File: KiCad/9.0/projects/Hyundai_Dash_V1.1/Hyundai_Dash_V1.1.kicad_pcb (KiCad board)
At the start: 2 copper layers, 109 x 64 mm, 30 parts, among them J1 +12V-GND, J10 GND-Fuel, J2 IGN-LSG-RSG-LS1-LS2, J3 C-CAN, J4 C-CAN, J5 C-CAN SPI, J6 B-CAN, J7 B-CAN, J8 B-CAN SPI, J9 Jumper Holder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

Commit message: KiCad: Hyundai_Dash_V1.1: remove jumper holder
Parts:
- removed J9: Jumper Holder, Connector_PinHeader_2.54mm:PinHeader_1x02_P2.54mm_Vertical

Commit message: KiCad: Hyundai_Dash_V1.1: reassign annotations
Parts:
- J2: value IGN-LSG-RSG-LS1-LS2 -> IGN-HS1-HS2-LS1-LS2
- renumbered J10 to J9
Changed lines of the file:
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@@
 	(net 55 "Net-(U2-I4)")
 	(net 56 "Net-(U2-I1)")
-	(net 57 "unconnected-(U3-QH&apos;-Pad9)")
-	(net 58 "Net-(J10-Pin_2)")
+	(net 57 "Net-(J9-Pin_2)")
+	(net 58 "unconnected-(U3-QH'-Pad9)")
 	(net 59 "unconnected-(U1-O6-Pad13)")
 	(net 60 "unconnected-(U1-I6-Pad6)")
@@
 		(property ki_fp_filters "Connector*:*_1x??_*")
 		(sheetname "/")
-		(sheetfile "Hyundai_Dash_V1.kicad_sch")
+		(sheetfile "Hyundai_Dash_V1.1.kicad_sch")
 		(attr through_hole exclude_from_bom)
 		(fp_line
@@
 		(property ki_fp_filters "R_*")
 		(sheetname "/")
-		(sheetfile "Hyundai_Dash_V1.kicad_sch")
+		(sheetfile "Hyundai_Dash_V1.1.kicad_sch")
 		(attr smd)
 		(fp_line
@@
 		(property ki_fp_filters "Connector*:*_1x??_*")
 		(sheetname "/")
-		(sheetfile "Hyundai_Dash_V1.kicad_sch")
+		(sheetfile "Hyundai_Dash_V1.1.kicad_sch")
 		(attr through_hole exclude_from_bom)
 		(fp_line
@@
 		(property ki_fp_filters "R_*")
 		(sheetname "/")
-		(sheetfile "Hyundai_Dash_V1.kicad_sch")
+		(sheetfile "Hyundai_Dash_V1.1.kicad_sch")
 		(attr smd)
 		(fp_line
@@
 			(layers "F.Cu" "F.Mask" "F.Paste")
 			(roundrect_rratio 0.204082)
-			(net 58 "Net-(J10-Pin_2)")
+			(net 57 "Net-(J9-Pin_2)")
 			(pintype "passive")
 		)
@@
 		(property ki_fp_filters "C_*")
 		(sheetname "/")
-		(sheetfile "Hyundai_Dash_V1.kicad_sch")
+		(sheetfile "Hyundai_Dash_V1.1.kicad_sch")
 		(attr smd)
 		(fp_line
@@
 		(property ki_fp_filters "TO?220*")
 		(sheetname "/")
-		(sheetfile "Hyundai_Dash_V1.kicad_sch")
+		(sheetfile "Hyundai_Dash_V1.1.kicad_sch")
 		(attr through_hole exclude_from_bom)
 		(fp_line
@@
 		(property ki_fp_filters "R_*")
 		(sheetname "/")
-		(sheetfile "Hyundai_Dash_V1.kicad_sch")
+		(sheetfile "Hyundai_Dash_V1.1.kicad_sch")
 		(attr smd)
 		(fp_line
@@
 			(layers "F.Cu" "F.Mask" "F.Paste")
 			(roundrect_rratio 0.204082)
-			(net 58 "Net-(J10-Pin_2)")
+			(net 57 "Net-(J9-Pin_2)")
 			(pintype "passive")
 		)
@@
 		(property ki_fp_filters "Connector*:*_1x??_*")
 		(sheetname "/")
-		(sheetfile "Hyundai_Dash_V1.kicad_sch")
+		(sheetfile "Hyundai_Dash_V1.1.kicad_sch")
 		(attr through_hole exclude_from_bom)
 		(fp_line
@@
 		(property ki_fp_filters "R_*")
 		(sheetname "/")
-		(sheetfile "Hyundai_Dash_V1.kicad_sch")
+		(sheetfile "Hyundai_Dash_V1.1.kicad_sch")
 		(attr smd)
 		(fp_line
@@
 			(layers "F.Cu" "F.Mask" "F.Paste")
 			(roundrect_rratio 0.204082)
-			(net 58 "Net-(J10-Pin_2)")
+			(net 57 "Net-(J9-Pin_2)")
 			(pintype "passive")
 		)
@@
 		(property ki_fp_filters "DIP*W7.62mm* SOIC*7.5x11.6mm*P1.27mm*")
 		(sheetname "/")
-		(sheetfile "Hyundai_Dash_V1.kicad_sch")
+		(sheetfile "Hyundai_Dash_V1.1.kicad_sch")
 		(attr through_hole exclude_from_bom)
 		(fp_line
@@
 		(property ki_fp_filters "R_*")
 		(sheetname "/")
-		(sheetfile "Hyundai_Dash_V1.kicad_sch")
+		(sheetfile "Hyundai_Dash_V1.1.kicad_sch")
 		(attr smd)
 		(fp_line
@@
 			(layers "F.Cu" "F.Mask" "F.Paste")
 			(roundrect_rratio 0.204082)
-			(net 58 "Net-(J10-Pin_2)")
+			(net 57 "Net-(J9-Pin_2)")
 			(pintype "passive")
 		)
@@
 		(descr "JST XH series connector, B2B-XH-A (http://www.jst-mfg.com/product/pdf/eng/eXH.pdf), generated with kicad-footprint-generator")
 		(tags "connector JST XH vertical")
-		(property "Reference" "J10"
+		(property "Reference" "J9"
 			(at 1.25 -3.55 0)
 			(layer "F.SilkS")
@@
 		(property ki_fp_filters "Connector*:*_1x??_*")
 		(sheetname "/")
-		(sheetfile "Hyundai_Dash_V1.kicad_sch")
+		(sheetfile "Hyundai_Dash_V1.1.kicad_sch")
 		(attr through_hole exclude_from_bom)
 		(fp_line
@@
 			(layers "*.Cu" "*.Mask")
 			(remove_unused_layers no)
-			(net 58 "Net-(J10-Pin_2)")
+			(net 57 "Net-(J9-Pin_2)")
 			(pinfunction "Pin_2")
 			(pintype "passive")
@@
 		(property ki_fp_filters "Connector*:*_1x??_*")
 		(sheetname "/")
-		(sheetfile "Hyundai_Dash_V1.kicad_sch")
+		(sheetfile "Hyundai_Dash_V1.1.kicad_sch")
 		(attr through_hole exclude_from_bom)
 		(fp_line
@@
 		(property ki_fp_filters "DIP*W7.62mm* SOIC*7.5x11.6mm*P1.27mm*")
 		(sheetname "/")
-		(sheetfile "Hyundai_Dash_V1.kicad_sch")
+		(sheetfile "Hyundai_Dash_V1.1.kicad_sch")
 		(attr through_hole exclude_from_bom)
 		(fp_line
@@
 		(property ki_fp_filters "R_*")
 		(sheetname "/")
-		(sheetfile "Hyundai_Dash_V1.kicad_sch")
+		(sheetfile "Hyundai_Dash_V1.1.kicad_sch")
 		(attr smd)
 		(fp_line
@@
 			(layers "F.Cu" "F.Mask" "F.Paste")
 			(roundrect_rratio 0.204082)
-			(net 58 "Net-(J10-Pin_2)")
+			(net 57 "Net-(J9-Pin_2)")
 			(pintype "passive")
 		)
@@
 		(property ki_fp_filters "Arduino*Nano*")
 		(sheetname "/")
-		(sheetfile "Hyundai_Dash_V1.kicad_sch")
+		(sheetfile "Hyundai_Dash_V1.1.kicad_sch")
 		(attr through_hole exclude_from_bom)
 		(fp_line
@@
 		(property ki_fp_filters "Connector*:*_1x??_*")
 		(sheetname "/")
-		(sheetfile "Hyundai_Dash_V1.kicad_sch")
+		(sheetfile "Hyundai_Dash_V1.1.kicad_sch")
 		(attr through_hole exclude_from_bom)
 		(fp_line
@@
 		(property ki_fp_filters "R_*")
 		(sheetname "/")
-		(sheetfile "Hyundai_Dash_V1.kicad_sch")
+		(sheetfile "Hyundai_Dash_V1.1.kicad_sch")
 		(attr smd)
 		(fp_line
@@
 			(layers "F.Cu" "F.Mask" "F.Paste")
 			(roundrect_rratio 0.204082)
-			(net 58 "Net-(J10-Pin_2)")
+			(net 57 "Net-(J9-Pin_2)")
 			(pintype "passive")
 		)
@@
 		(property ki_fp_filters "Connector*:*_1x??_*")
 		(sheetname "/")
-		(sheetfile "Hyundai_Dash_V1.kicad_sch")
+		(sheetfile "Hyundai_Dash_V1.1.kicad_sch")
 		(attr through_hole exclude_from_bom)
 		(fp_line
@@
 		(property ki_fp_filters "TO?92*")
 		(sheetname "/")
-		(sheetfile "Hyundai_Dash_V1.kicad_sch")
+		(sheetfile "Hyundai_Dash_V1.1.kicad_sch")
 		(attr through_hole)
 		(fp_line
@@
 		(property ki_fp_filters "Connector*:*_1x??_*")
 		(sheetname "/")
-		(sheetfile "Hyundai_Dash_V1.kicad_sch")
+		(sheetfile "Hyundai_Dash_V1.1.kicad_sch")
 		(attr through_hole exclude_from_bom)
 		(fp_line
@@
 			)
 		)
-		(property "Value" "IGN-LSG-RSG-LS1-LS2"
+		(property "Value" "IGN-HS1-HS2-LS1-LS2"
 			(at 5 4.6 0)
 			(layer "F.SilkS")
@@
 		(property ki_fp_filters "Connector*:*_1x??_*")
 		(sheetname "/")
-		(sheetfile "Hyundai_Dash_V1.kicad_sch")
+		(sheetfile "Hyundai_Dash_V1.1.kicad_sch")
 		(attr through_hole)
 		(fp_line
@@
 		(property ki_fp_filters "R_*")
 		(sheetname "/")
-		(sheetfile "Hyundai_Dash_V1.kicad_sch")
+		(sheetfile "Hyundai_Dash_V1.1.kicad_sch")
 		(attr smd)
 		(fp_line
@@
 			(layers "F.Cu" "F.Mask" "F.Paste")
 			(roundrect_rratio 0.204082)
-			(net 58 "Net-(J10-Pin_2)")
+			(net 57 "Net-(J9-Pin_2)")
 			(pintype "passive")
 		)
@@
 		(property ki_fp_filters "TO?92*")
 		(sheetname "/")
-		(sheetfile "Hyundai_Dash_V1.kicad_sch")
+		(sheetfile "Hyundai_Dash_V1.1.kicad_sch")
 		(attr through_hole)
 		(fp_line
@@
 		(property ki_fp_filters "*Buzzer*")
 		(sheetname "/")
-		(sheetfile "Hyundai_Dash_V1.kicad_sch")
+		(sheetfile "Hyundai_Dash_V1.1.kicad_sch")
 		(attr through_hole exclude_from_bom)
 		(fp_circle
@@
 		(property ki_fp_filters "R_*")
 		(sheetname "/")
-		(sheetfile "Hyundai_Dash_V1.kicad_sch")
+		(sheetfile "Hyundai_Dash_V1.1.kicad_sch")
 		(attr smd)
 		(fp_line
@@
 			(layers "F.Cu" "F.Mask" "F.Paste")
 			(roundrect_rratio 0.204082)
-			(net 58 "Net-(J10-Pin_2)")
+			(net 57 "Net-(J9-Pin_2)")
 			(pintype "passive")
 		)
@@
 		(property ki_fp_filters "R_*")
 		(sheetname "/")
-		(sheetfile "Hyundai_Dash_V1.kicad_sch")
+		(sheetfile "Hyundai_Dash_V1.1.kicad_sch")
 		(attr smd)
 		(fp_line
@@
 		(property ki_fp_filters "DIP*W7.62mm* SOIC*3.9x9.9mm*P1.27mm* TSSOP*4.4x5mm*P0.65mm* SOIC*5.3x10.2mm*P1.27mm* SOIC*7.5x10.3mm*P1.27mm*")
 		(sheetname "/")
-		(sheetfile "Hyundai_Dash_V1.kicad_sch")
+		(sheetfile "Hyundai_Dash_V1.1.kicad_sch")
 		(attr through_hole exclude_from_bom)
 		(fp_line
@@
 			(layers "*.Cu" "*.Mask")
 			(remove_unused_layers no)
-			(net 57 "unconnected-(U3-QH&apos;-Pad9)")
+			(net 58 "unconnected-(U3-QH'-Pad9)")
 			(pinfunction "QH'")
 			(pintype "output+no_connect")
@@
 		(property ki_fp_filters "R_*")
 		(sheetname "/")
-		(sheetfile "Hyundai_Dash_V1.kicad_sch")
+		(sheetfile "Hyundai_Dash_V1.1.kicad_sch")
 		(attr smd)
 		(fp_line
@@
 		(locked yes)
 		(layer "F.Cu")
-		(net 58)
+		(net 57)
 	)
 	(segment
@@
 		(locked yes)
 		(layer "F.Cu")
-		(net 58)
+		(net 57)
 	)
 	(segment
@@
 		(locked yes)
 		(layer "F.Cu")
-		(net 58)
+		(net 57)
 	)
 	(segment
@@
 		(locked yes)
 		(layer "F.Cu")
-		(net 58)
+		(net 57)
 	)
 	(segment
@@
 		(locked yes)
 		(layer "F.Cu")
-		(net 58)
+		(net 57)
 	)
 	(segment
@@
 		(locked yes)
 		(layer "F.Cu")
-		(net 58)
+		(net 57)
 	)
 	(segment
@@
 		(locked yes)
 		(layer "F.Cu")
-		(net 58)
+		(net 57)
 	)
 	(segment
@@
 		(locked yes)
 		(layer "F.Cu")
-		(net 58)
+		(net 57)
 	)
 	(segment
@@
 		(locked yes)
 		(layer "F.Cu")
-		(net 58)
+		(net 57)
 	)
 	(segment
@@
 		(locked yes)
 		(layer "F.Cu")
-		(net 58)
+		(net 57)
 	)
 	(segment
@@
 		(locked yes)
 		(layer "F.Cu")
-		(net 58)
+		(net 57)
 	)
 	(segment

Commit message: KiCad: Hyundai_Dash_V1.1: update U1-U3 footprints to non-socketed versions
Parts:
- U1, U2: footprint Package_DIP:DIP-18_W7.62mm_Socket -> Package_DIP:DIP-18_W7.62mm
- U3: footprint Package_DIP:DIP-16_W7.62mm_Socket -> Package_DIP:DIP-16_W7.62mm
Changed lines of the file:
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@@
 		)
 	)
-	(footprint "Package_DIP:DIP-18_W7.62mm_Socket"
+	(footprint "Package_DIP:DIP-18_W7.62mm"
 		(locked yes)
 		(layer "F.Cu")
 		(at 205.501824 61.419772)
-		(descr "18-lead though-hole mounted DIP package, row spacing 7.62mm (300 mils), Socket")
-		(tags "THT DIP DIL PDIP 2.54mm 7.62mm 300mil Socket")
+		(descr "18-lead though-hole mounted DIP package, row spacing 7.62mm (300 mils)")
+		(tags "THT DIP DIL PDIP 2.54mm 7.62mm 300mil")
 		(property "Reference" "U2"
 			(at 3.81 -2.33 0)
@@
 		)
 		(property "Value" "ULN2803A"
-			(at 3.81 -3.72 0)
+			(at 3.748176 -3.919772 0)
 			(layer "F.SilkS")
 			(effects
@@
 			)
 		)
-		(property "Datasheet" "http://www.ti.com/lit/ds/symlink/uln2803a.pdf"
+		(property "Datasheet" ""
 			(at 0 0 0)
 			(layer "F.Fab")
@@
 			)
 		)
-		(property "Description" "Darlington Transistor Arrays, SOIC18/DIP18"
+		(property "Description" ""
 			(at 0 0 0)
 			(layer "F.Fab")
@@
 		(sheetname "/")
 		(sheetfile "Hyundai_Dash_V1.1.kicad_sch")
-		(attr through_hole exclude_from_bom)
+		(attr through_hole)
 		(fp_line
 			(start 1.16 -1.33)
@@
 			(layer "F.SilkS")
 		)
-		(fp_rect
-			(start -1.33 -1.39)
-			(end 8.95 21.71)
-			(stroke
-				(width 0.12)
-				(type solid)
-			)
-			(fill no)
-			(layer "F.SilkS")
-		)
 		(fp_arc
 			(start 4.81 -1.33)
@@
 		)
 		(fp_rect
-			(start -1.52 -1.58)
-			(end 9.14 21.9)
+			(start -1.06 -1.52)
+			(end 8.67 21.84)
 			(stroke
 				(width 0.05)
@@
 			(layer "F.Fab")
 		)
-		(fp_rect
-			(start -1.27 -1.33)
-			(end 8.89 21.65)
-			(stroke
-				(width 0.1)
-				(type solid)
-			)
-			(fill no)
-			(layer "F.Fab")
-		)
 		(fp_text user "${REFERENCE}"
 			(at 3.81 10.16 90)
@@
 		)
 		(embedded_fonts no)
-		(model "${KICAD9_3DMODEL_DIR}/Package_DIP.3dshapes/DIP-18_W7.62mm_Socket.step"
+		(model "${KICAD9_3DMODEL_DIR}/Package_DIP.3dshapes/DIP-18_W7.62mm.step"
 			(offset
 				(xyz 0 0 0)
@@
 		)
 	)
-	(footprint "Package_DIP:DIP-18_W7.62mm_Socket"
+	(footprint "Package_DIP:DIP-18_W7.62mm"
 		(locked yes)
 		(layer "F.Cu")
 		(at 169.26 81.62 90)
-		(descr "18-lead though-hole mounted DIP package, row spacing 7.62mm (300 mils), Socket")
-		(tags "THT DIP DIL PDIP 2.54mm 7.62mm 300mil Socket")
+		(descr "18-lead though-hole mounted DIP package, row spacing 7.62mm (300 mils)")
+		(tags "THT DIP DIL PDIP 2.54mm 7.62mm 300mil")
 		(property "Reference" "U1"
 			(at 3.81 -2.33 90)
@@
 		)
 		(property "Value" "ULN2803A"
-			(at 10.12 3.24 180)
+			(at 9.62 2.49 180)
 			(layer "F.SilkS")
 			(effects
@@
 			)
 		)
-		(property "Datasheet" "http://www.ti.com/lit/ds/symlink/uln2803a.pdf"
+		(property "Datasheet" ""
 			(at 0 0 90)
 			(layer "F.Fab")
@@
 			)
 		)
-		(property "Description" "Darlington Transistor Arrays, SOIC18/DIP18"
+		(property "Description" ""
 			(at 0 0 90)
 			(layer "F.Fab")
@@
 		(sheetname "/")
 		(sheetfile "Hyundai_Dash_V1.1.kicad_sch")
-		(attr through_hole exclude_from_bom)
+		(attr through_hole)
 		(fp_line
 			(start 6.46 -1.33)
@@
 			(layer "F.SilkS")
 		)
-		(fp_rect
-			(start -1.33 -1.39)
-			(end 8.95 21.71)
-			(stroke
-				(width 0.12)
-				(type solid)
-			)
-			(fill no)
-			(layer "F.SilkS")
-		)
 		(fp_arc
 			(start 4.81 -1.33)
@@
 		)
 		(fp_rect
-			(start -1.52 -1.58)
-			(end 9.14 21.9)
+			(start -1.06 -1.52)
+			(end 8.67 21.84)
 			(stroke
 				(width 0.05)
@@
 			(layer "F.Fab")
 		)
-		(fp_rect
-			(start -1.27 -1.33)
-			(end 8.89 21.65)
-			(stroke
-				(width 0.1)
-				(type solid)
-			)
-			(fill no)
-			(layer "F.Fab")
-		)
 		(fp_text user "${REFERENCE}"
-			(at 3.81 10.16 0)
+			(at 3.81 10.16 180)
 			(layer "F.Fab")
 			(effects
@@
 		)
 		(embedded_fonts no)
-		(model "${KICAD9_3DMODEL_DIR}/Package_DIP.3dshapes/DIP-18_W7.62mm_Socket.step"
+		(model "${KICAD9_3DMODEL_DIR}/Package_DIP.3dshapes/DIP-18_W7.62mm.step"
 			(offset
 				(xyz 0 0 0)
@@
 		)
 	)
-	(footprint "Package_DIP:DIP-16_W7.62mm_Socket"
+	(footprint "Package_DIP:DIP-16_W7.62mm"
 		(locked yes)
 		(layer "F.Cu")
 		(at 202 79.2 180)
-		(descr "16-lead though-hole mounted DIP package, row spacing 7.62mm (300 mils), Socket")
-		(tags "THT DIP DIL PDIP 2.54mm 7.62mm 300mil Socket")
+		(descr "16-lead though-hole mounted DIP package, row spacing 7.62mm (300 mils)")
+		(tags "THT DIP DIL PDIP 2.54mm 7.62mm 300mil")
 		(property "Reference" "U3"
-			(at 3.81 20.110228 0)
-			(unlocked yes)
+			(at 3.75 20.2 180)
 			(layer "F.SilkS")
 			(effects
@@
 		)
 		(property "Value" "74HC595"
-			(at 3.81 21.500228 180)
+			(at 3.75 21.7 180)
 			(layer "F.SilkS")
 			(effects
@@
 			)
 		)
-		(property "Datasheet" "http://www.ti.com/lit/ds/symlink/sn74hc595.pdf"
-			(at 0 0 0)
+		(property "Datasheet" ""
+			(at 0 0 180)
 			(layer "F.Fab")
 			(hide yes)
@@
 			)
 		)
-		(property "Description" "8-bit serial in/out Shift Register 3-State Outputs"
-			(at 0 0 0)
+		(property "Description" ""
+			(at 0 0 180)
 			(layer "F.Fab")
 			(hide yes)
@@
 		(sheetname "/")
 		(sheetfile "Hyundai_Dash_V1.1.kicad_sch")
-		(attr through_hole exclude_from_bom)
+		(attr through_hole)
 		(fp_line
 			(start 6.46 19.11)
@@
 			(layer "F.SilkS")
 		)
-		(fp_rect
-			(start -1.33 -1.39)
-			(end 8.95 19.17)
-			(stroke
-				(width 0.12)
-				(type solid)
-			)
-			(fill no)
-			(layer "F.SilkS")
-		)
 		(fp_arc
 			(start 4.81 -1.33)
@@
 		)
 		(fp_rect
-			(start -1.52 -1.58)
-			(end 9.14 19.36)
+			(start -1.06 -1.52)
+			(end 8.67 19.3)
 			(stroke
 				(width 0.05)
@@
 			(layer "F.Fab")
 		)
-		(fp_rect
-			(start -1.27 -1.33)
-			(end 8.89 19.11)
-			(stroke
-				(width 0.1)
-				(type solid)
-			)
-			(fill no)
-			(layer "F.Fab")
-		)
 		(fp_text user "${REFERENCE}"
-			(at 3.81 8.89 90)
+			(at 3.81 8.89 270)
 			(layer "F.Fab")
 			(effects
@@
 		)
 		(embedded_fonts no)
-		(model "${KICAD9_3DMODEL_DIR}/Package_DIP.3dshapes/DIP-16_W7.62mm_Socket.step"
+		(model "${KICAD9_3DMODEL_DIR}/Package_DIP.3dshapes/DIP-16_W7.62mm.step"
 			(offset
 				(xyz 0 0 0)

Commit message: KiCad: Hyundai_Dash_V1.1: update silkscreen markings
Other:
- board text added: "Hyundai Dash V1.1"
- board text added: "github.com/eymenyg/hyundai_dash_v1"
- board text removed: "Hyundai Dash V1"

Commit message: KiCad: Hyundai_Dash_V1.1: fix C1 positioning and R4 connection width
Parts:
- moved C1 2.97 mm to (195.2, 83.0)
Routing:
- net +5V: track 106.9 -> 102.3 mm
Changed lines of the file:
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@@
 	(footprint "Capacitor_SMD:C_0603_1608Metric"
 		(layer "F.Cu")
-		(at 198.19 83.199772)
+		(at 195.225 83)
 		(descr "Capacitor SMD 0603 (1608 Metric), square (rectangular) end terminal, IPC-7351 nominal, (Body size source: IPC-SM-782 page 76, https://www.pcb-3d.com/wordpress/wp-content/uploads/ipc-sm-782a_amendment_1_and_2.pdf), generated with kicad-footprint-generator")
 		(tags "capacitor")
@@
 	)
 	(segment
-		(start 197.415 83.199772)
-		(end 196.699772 83.199772)
+		(start 123.116614 92.306195)
+		(end 123.193805 92.306195)
 		(width 0.2)
 		(layer "F.Cu")
@@
 	)
 	(segment
-		(start 196.699772 83.199772)
-		(end 194.38 80.88)
+		(start 164.68 92.38)
+		(end 165 92.38)
 		(width 0.2)
 		(layer "F.Cu")
@@
 	)
 	(segment
-		(start 194.38 80.88)
-		(end 194.38 79.2)
+		(start 154.04 81.74)
+		(end 155.3 83)
 		(width 0.2)
 		(layer "F.Cu")
@@
 	)
 	(segment
-		(start 123.116614 92.306195)
-		(end 123.193805 92.306195)
+		(start 155.3 83)
+		(end 164.68 92.38)
 		(width 0.2)
 		(layer "F.Cu")
@@
 	)
 	(segment
-		(start 164.68 92.38)
-		(end 165 92.38)
+		(start 194.45 83)
+		(end 155.3 83)
 		(width 0.2)
 		(layer "F.Cu")
@@
 	)
 	(segment
-		(start 154.04 81.74)
-		(end 164.68 92.38)
+		(start 194.38 79.2)
+		(end 194.38 82.93)
 		(width 0.2)
 		(layer "F.Cu")
@@
 	)
 	(segment
-		(start 197.415 83.199772)
-		(end 155.499772 83.199772)
+		(start 194.38 82.93)
+		(end 194.45 83)
 		(width 0.2)
 		(layer "F.Cu")
@@
 		(start 223.9625 53.9625)
 		(end 223.9625 56.09)
-		(width 0.2)
+		(width 0.4)
 		(layer "F.Cu")
 		(net 57)

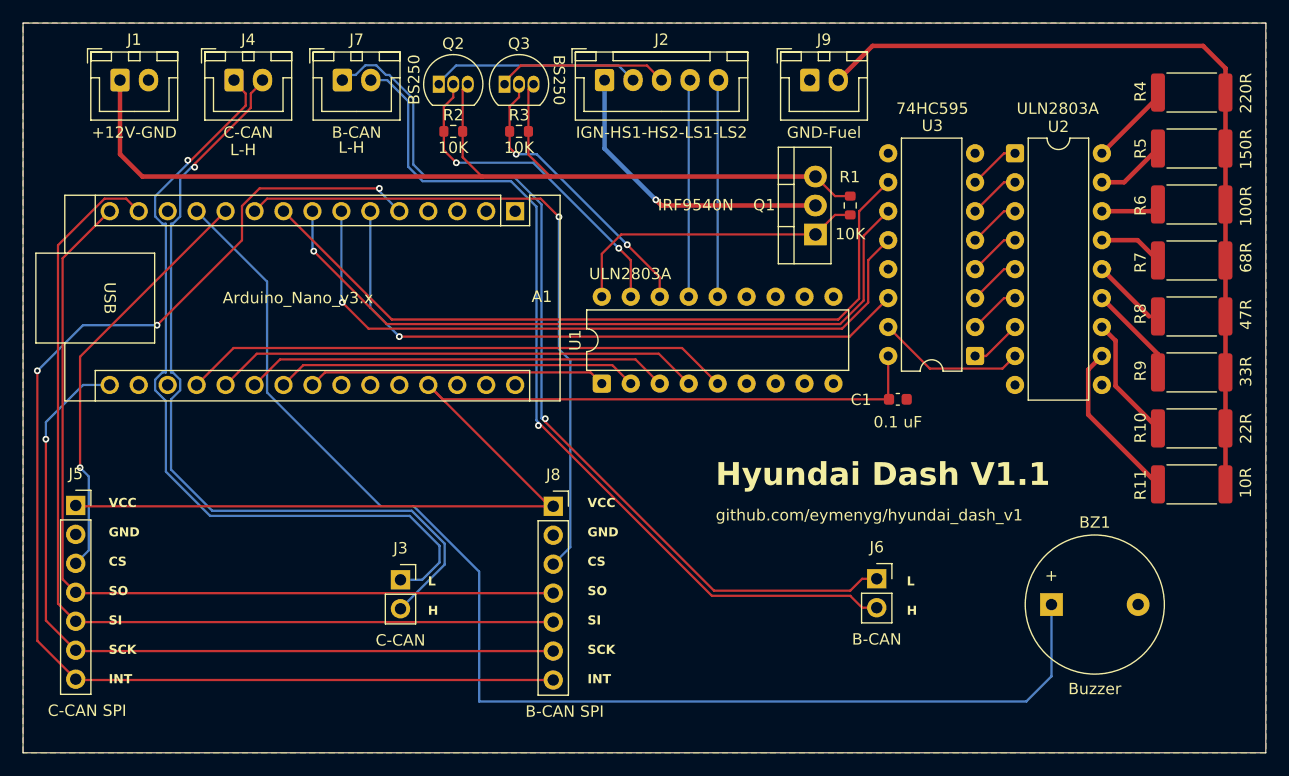
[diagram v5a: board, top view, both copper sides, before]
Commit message: KiCad: Hyundai_Dash_V1.1: fix DRC warnings
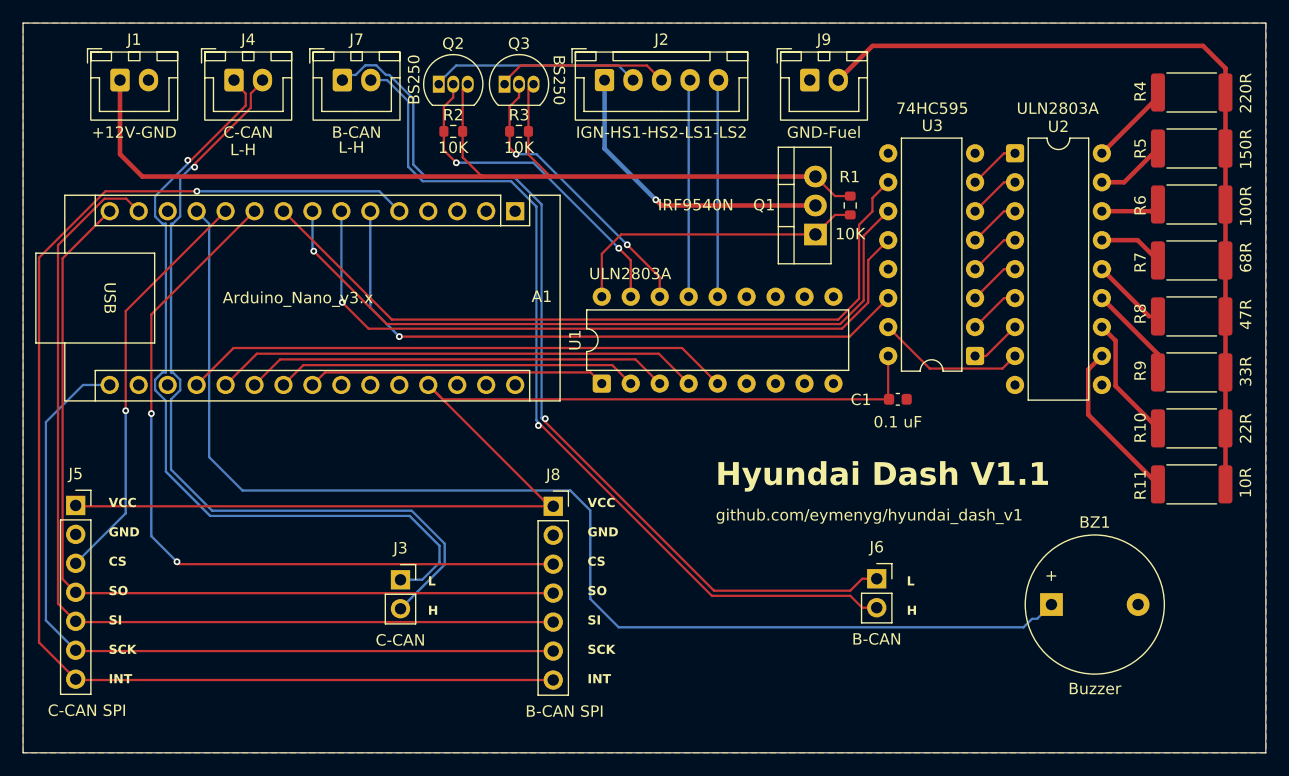
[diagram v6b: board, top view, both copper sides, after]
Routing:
- net /CAN_CS_B: track 59.3 -> 68.5 mm, vias 1 -> 2
- net Net-(A1-D9): track 112.4 -> 107.5 mm
- net /CAN_INT: track 111.5 -> 115.0 mm, vias 3 -> 1
- net /CAN_CS_C: track 37.0 -> 36.3 mm
- net /SCK: vias 1 -> 0
